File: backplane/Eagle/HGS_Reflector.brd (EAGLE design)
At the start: 100 x 100 mm, 3 parts, among them J1 U.FL, U1 TQP3M9037, X1 MINI-USB-32005-201

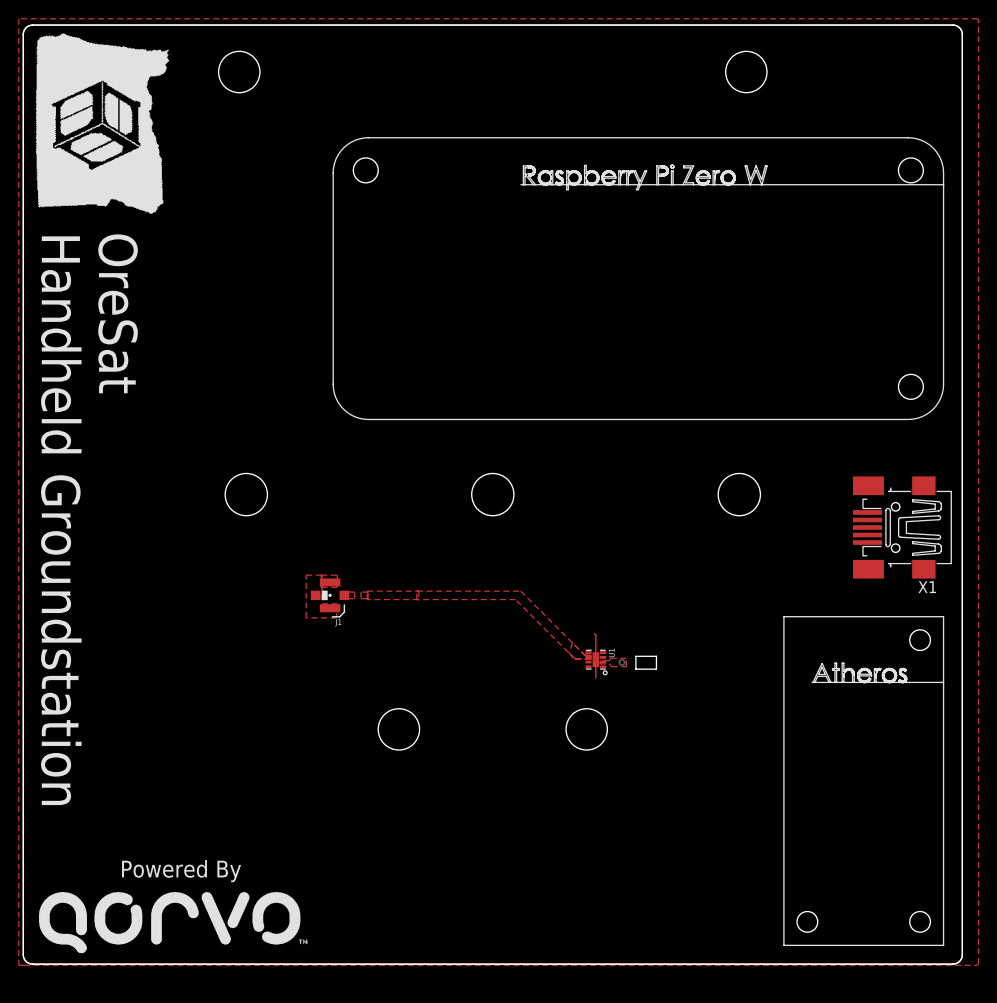
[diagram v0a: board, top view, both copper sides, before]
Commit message: updated hgs mockup
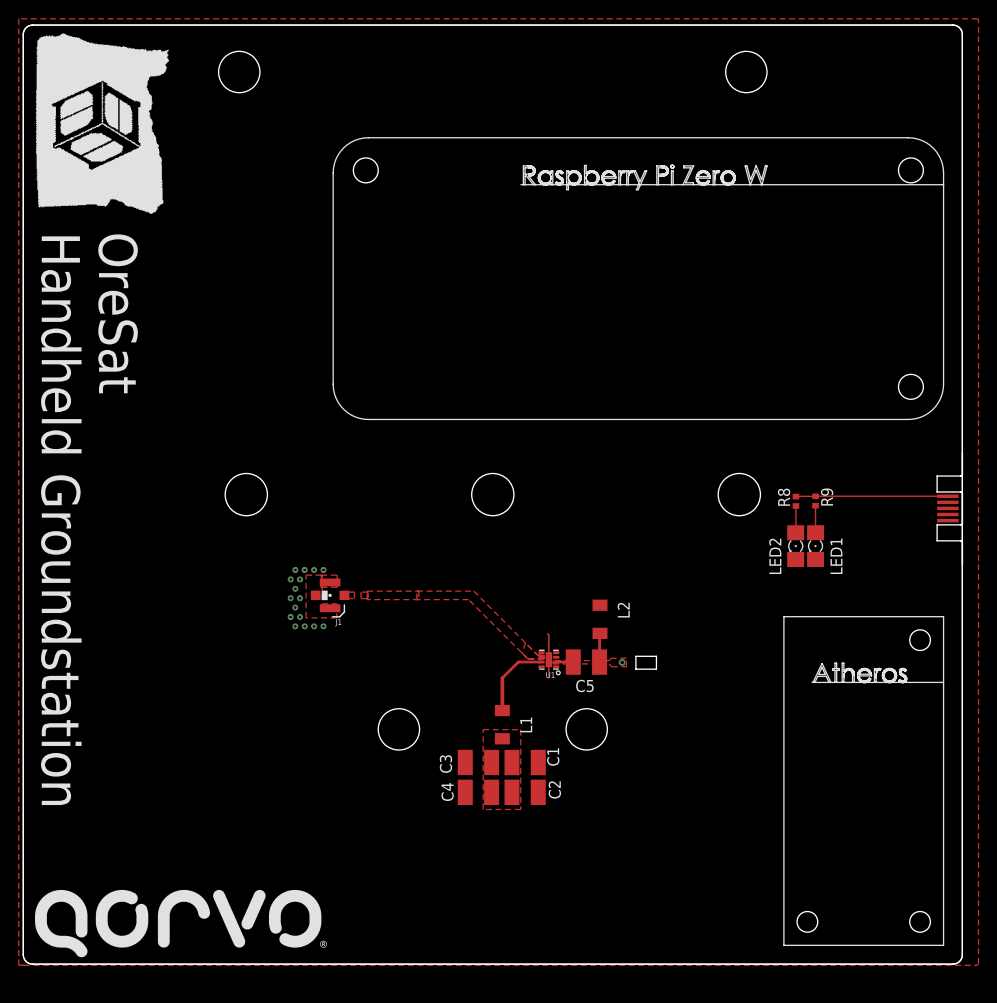
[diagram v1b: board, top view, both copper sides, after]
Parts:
- removed X1: MINI-USB-32005-201, con-cypressindustries:32005-201
- added C1, C2, C3, C4, C5: (no value), rcl:C1210
- added L1, L2: (no value), rcl:L3216C
- added LED1, LED2: (no value), eagle-ltspice:LED_1206
- added R8, R9: (no value), rcl:R0402
- added U$1: PCB_MICRO_USB_BSS_1, USB_pcb_connectors:USB_TYPE_B_SS_1
- moved U1 5.00 mm to (55.5, 31.9)
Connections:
- new net N$10: LED1.A, R9.1
- new net N$11: R8.2, R9.2, U$1.1
- new net N$5: L1.1, U1.7
- new net N$6: C1.1, C2.1, C3.1, C4.1, L1.2
- new net N$7: C5.1, L2.2
- new net N$8: C5.2, U1.2
- new net N$9: LED2.A, R8.1
- net GND: now also C1.2, C2.2, C3.2, C4.2, L2.1, LED1.C, LED2.C
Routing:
- net N$11: track 0.00 -> 16.2 mm
- net N$5: track 0.00 -> 8.34 mm
- net N$7: track 0.00 -> 3.08 mm
- net N$10: track 0.00 -> 2.88 mm
- net N$9: track 0.00 -> 2.86 mm
- net N$8: track 0.00 -> 1.82 mm
- net GND: vias 0 -> 16
- added copper zone on layer 1, net N$6
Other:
- board text removed: "Powered By"
